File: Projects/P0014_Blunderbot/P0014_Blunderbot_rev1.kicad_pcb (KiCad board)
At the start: 2 copper layers, 63.5 x 25.4 mm, 19 parts, among them J1 22-03-5035, J2 22-03-5035, J3 70553-0037, J4 70553-0037, J5 CONN_01X04, J6 CONN_01X04, P1 CONN_02X03, U1 TC7W241FUTE12LF, U2 MIC5219-5.0YM5-TR, U3 MIC5219-5.0YM5-TR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

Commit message: layout nearly done
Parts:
- added S1: MHSS1105, Pin_Headers:Pin_Header_Straight_1x03, F.Cu at (129.5, 89.5)
- moved U3 22.5 mm to (140.6, 107.0)
- moved C2 19.7 mm to (145.3, 105.3), turned to 90 degrees
- moved RP1 18.2 mm to (137.5, 90.8)
- moved U4 14.2 mm to (151.9, 101.5), turned to 0 degrees
- moved C4 14.1 mm to (159.5, 106.6), turned to 90 degrees
- moved C5 11.8 mm to (140.2, 97.7)
- moved C1 8.52 mm to (133.4, 102.9), turned to 0 degrees
- moved U2 8.42 mm to (124.6, 95.6), turned to 180 degrees
- moved C3 4.09 mm to (124.5, 100.9), turned to 270 degrees
- moved D2 3.42 mm to (129.5, 93.3), turned to 180 degrees
- moved U1 3.32 mm to (141.4, 100.9)
- moved J5 2.54 mm to (177.8, 95.2)
- moved J6 2.54 mm to (119.4, 102.9)
- moved J3 2.54 mm to (163.8, 92.7)
- moved J4 2.54 mm to (168.9, 105.4)
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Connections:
- C1 pad 1: /9-12V_IN -> /9-10V_IN
- J1 pad 2: /9-12V_IN -> /9-10V_IN
- J2 pad 2: /9-12V_IN -> /9-10V_IN
- J3 pad 2: /MISO -> /MOSI/PWM2
- J4 pad 2: /PWM1 -> /MISO/PWM1
- P1 pad 1: /MISO -> /MISO/PWM1
- P1 pad 4: /MOSI -> /MOSI/PWM2
- U1 pad 5: /PWM1 -> /TX
- U2 pad 1: /9-12V_IN -> /9-10V_IN
- U2 pad 3: /9-12V_IN -> Net-(S1-Pad3)
- U3 pad 1: /9-12V_IN -> /9-10V_IN
- U4 pad 10: /SERVO_EN -> /TXDEN
- U4 pad 12: /PWM1 -> /TX
- U4 pad 13: /TXDEN -> /SERVO_EN
- U4 pad 7: /MOSI -> /MOSI/PWM2
- U4 pad 8: /MISO -> /MISO/PWM1
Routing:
- net GND: track 0.00 -> 148.0 mm, vias 0 -> 5
- net /VCC: track 4.39 -> 76.6 mm, vias 0 -> 2
- net /9-10V_IN: track 0.00 -> 40.6 mm, vias 0 -> 2
- net /MISO: track 35.4 -> 0.00 mm, vias 1 -> 0
- net /PWM1: track 31.9 -> 0.00 mm
- net /TTL_BUS: track 4.40 -> 36.3 mm, vias 0 -> 2
- net /MOSI/PWM2: track 0.00 -> 29.4 mm
- net /MISO/PWM1: track 0.00 -> 29.1 mm, vias 0 -> 2
- net Net-(D1-Pad1): track 0.00 -> 24.0 mm, vias 0 -> 1
- net /TRIG1: track 48.4 -> 24.5 mm
- net /VBB: track 20.0 -> 41.5 mm, vias 0 -> 1
- net /TRIG2: track 20.6 -> 33.7 mm
- net /TX: track 0.00 -> 12.6 mm, vias 0 -> 2
- net /ECHO2: track 24.6 -> 37.1 mm
- net /TXDEN: track 4.67 -> 16.9 mm
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- added copper zone on B.Cu, net /9-10V_IN
- added copper zone on B.Cu, net /VBB
- added copper zone on B.Cu, net /VCC
- added copper zone on B.Cu, net GND
- added copper zone on F.Cu, net GND
- added copper zone on B.Cu, net Net-(C3-Pad1)
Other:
- board text added: "9-10VIN"
- board text added: "Blunderbot"
- board text added: "Designed by Max Prokopenko"
- board text added: "OpenRobotics.ca"
- board text added: "P0014 rev1"
- board text added: "PA0-SERVO_EN PA1-TX PA2-RX PA3-TXDEN PA4-SCK PA5-MISO/PWM1 PA6-MOSI/PWM2 PA7-TRIG1 PB0-ECHO1 PB1-TRIG2 PB2-ECHO2 PB3-~RESET"
- board text removed: "9-11VIN"

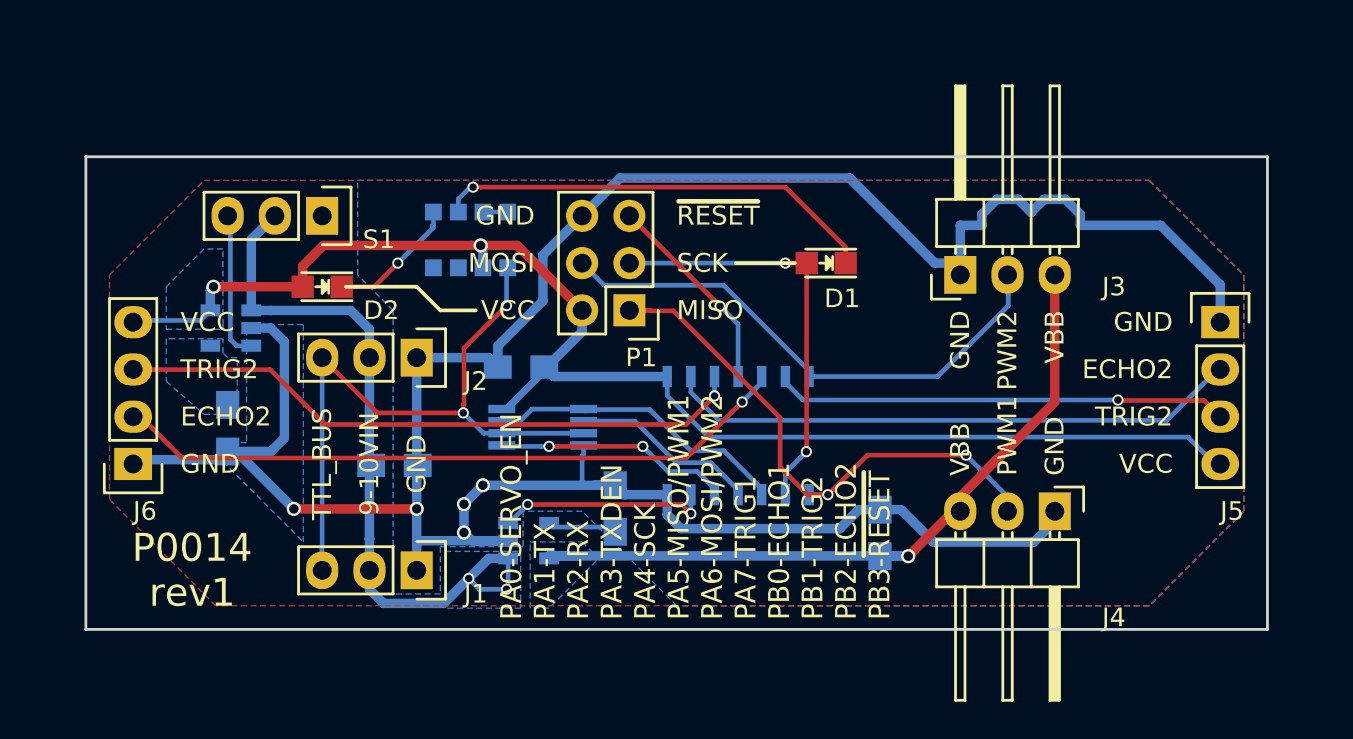
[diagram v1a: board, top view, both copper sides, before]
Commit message: layout first pass finished, need to update gerbers for seeed
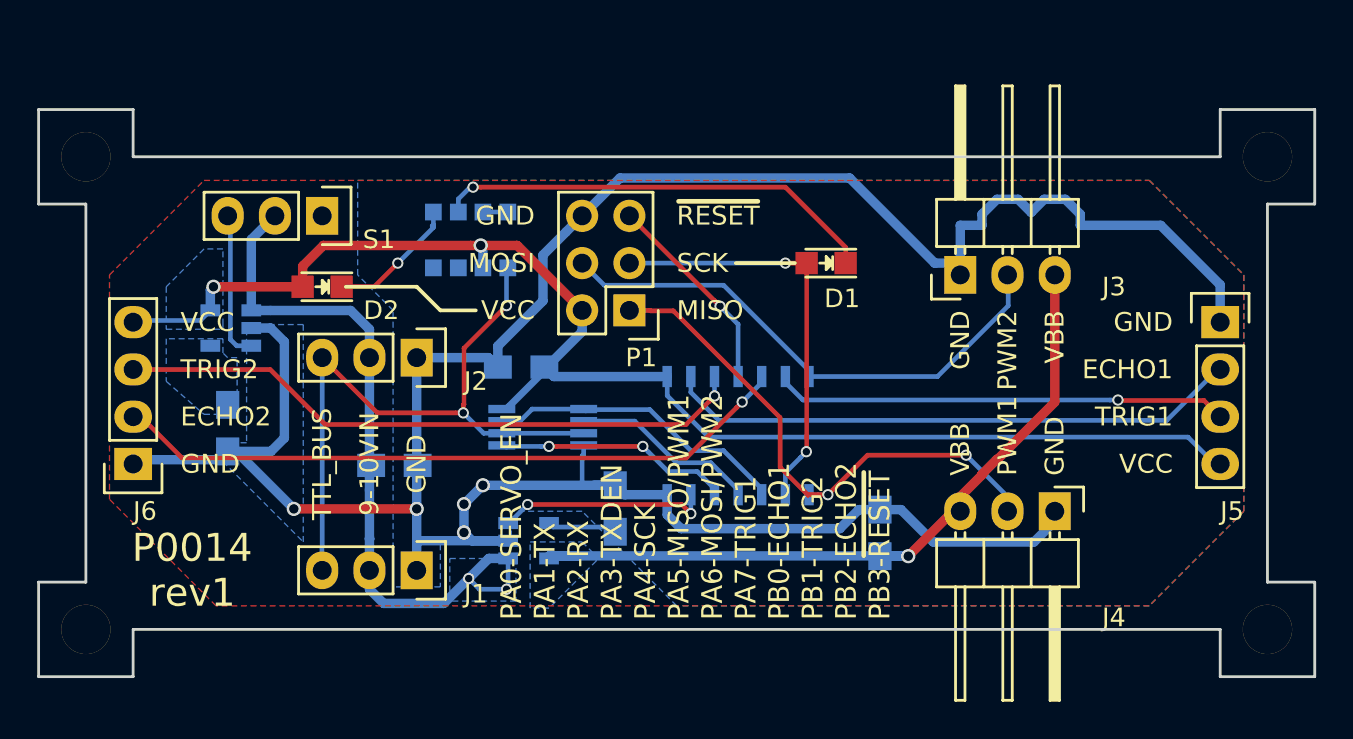
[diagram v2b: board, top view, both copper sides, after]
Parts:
- added REF**: modular8_mounting_hole, open_robotics:modular8_mounting_hole, F.Cu at (180.3, 86.4)
- added REF**: modular8_mounting_hole, open_robotics:modular8_mounting_hole, F.Cu at (180.3, 111.8)
- added REF**: modular8_mounting_hole, open_robotics:modular8_mounting_hole, F.Cu at (116.8, 111.8)
- added REF**: modular8_mounting_hole, open_robotics:modular8_mounting_hole, F.Cu at (116.8, 86.4)
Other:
- board size 63.5 x 25.4 mm -> 68.6 x 30.5 mm
- net class power: clearance 0.254 -> 0.2
- board text added: "ECHO1"
- board text added: "TRIG1"
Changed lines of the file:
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@@
 (kicad_pcb (version 4) (host pcbnew 4.0.1-stable)
   (general
-    (links 59)
+    (links 0)
     (no_connects 0)
-    (area 114.217667 79.240999 182.962334 113.799001)
+    (area 107.231666 81.834999 189.948335 116.285001)
     (thickness 1.6)
-    (drawings 37)
+    (drawings 53)
     (tracks 304)
     (zones 0)
-    (modules 20)
+    (modules 24)
     (nets 25)
   )
   (page A4)
   (layers
-    (0 F.Cu signal hide)
+    (0 F.Cu signal)
     (31 B.Cu signal)
     (32 B.Adhes user hide)
@@
     (34 B.Paste user hide)
     (35 F.Paste user hide)
-    (36 B.SilkS user)
-    (37 F.SilkS user hide)
+    (36 B.SilkS user hide)
+    (37 F.SilkS user)
     (38 B.Mask user hide)
     (39 F.Mask user hide)
@@
     (pad_to_mask_clearance 0.2)
     (aux_axis_origin 0 0)
-    (visible_elements 7FFFBE7F)
+    (visible_elements 7FFFFE7F)
     (pcbplotparams
-      (layerselection 0x00030_80000001)
-      (usegerberextensions false)
+      (layerselection 0x010f0_80000001)
+      (usegerberextensions true)
       (excludeedgelayer true)
       (linewidth 0.100000)
@@
       (outputformat 1)
       (mirror false)
-      (drillshape 1)
+      (drillshape 0)
       (scaleselection 1)
       (outputdirectory ""))
@@
   )
   (net_class power ""
-    (clearance 0.254)
+    (clearance 0.2)
     (trace_width 0.508)
     (via_dia 0.762)
@@
     )
   )
-  (gr_text Blunderbot (at 170.434 89.154) (layer B.SilkS)
+  (module open_robotics:modular8_mounting_hole (layer F.Cu)
+    (at 180.34 86.36)
+    (fp_text reference REF** (at 0 0.5) (layer F.SilkS) hide
+      (effects (font (size 1 1) (thickness 0.15)))
+    )
+    (fp_text value modular8_mounting_hole (at 0 -0.5) (layer F.Fab) hide
+      (effects (font (size 1 1) (thickness 0.15)))
+    )
+    (pad 1 thru_hole circle (at 0 0) (size 2.65 2.65) (drill 2.65) (layers *.Cu *.Mask F.SilkS))
+  )
+  (module open_robotics:modular8_mounting_hole (layer F.Cu)
+    (at 180.34 111.76)
+    (fp_text reference REF** (at 0 0.5) (layer F.SilkS) hide
+      (effects (font (size 1 1) (thickness 0.15)))
+    )
+    (fp_text value modular8_mounting_hole (at 0 -0.5) (layer F.Fab) hide
+      (effects (font (size 1 1) (thickness 0.15)))
+    )
+    (pad 1 thru_hole circle (at 0 0) (size 2.65 2.65) (drill 2.65) (layers *.Cu *.Mask F.SilkS))
+  )
+  (module open_robotics:modular8_mounting_hole (layer F.Cu)
+    (at 116.84 111.76)
+    (fp_text reference REF** (at 0 0.5) (layer F.SilkS) hide
+      (effects (font (size 1 1) (thickness 0.15)))
+    )
+    (fp_text value modular8_mounting_hole (at 0 -0.5) (layer F.Fab) hide
+      (effects (font (size 1 1) (thickness 0.15)))
+    )
+    (pad 1 thru_hole circle (at 0 0) (size 2.65 2.65) (drill 2.65) (layers *.Cu *.Mask F.SilkS))
+  )
+  (module open_robotics:modular8_mounting_hole (layer F.Cu)
+    (at 116.84 86.36)
+    (fp_text reference REF** (at 0 0.5) (layer F.SilkS) hide
+      (effects (font (size 1 1) (thickness 0.15)))
+    )
+    (fp_text value modular8_mounting_hole (at 0 -0.5) (layer F.Fab) hide
+      (effects (font (size 1 1) (thickness 0.15)))
+    )
+    (pad 1 thru_hole circle (at 0 0) (size 2.65 2.65) (drill 2.65) (layers *.Cu *.Mask F.SilkS))
+  )
+  (gr_line (start 180.34 109.22) (end 180.34 88.9) (layer Edge.Cuts) (width 0.15))
+  (gr_line (start 182.88 109.22) (end 180.34 109.22) (layer Edge.Cuts) (width 0.15))
+  (gr_line (start 182.88 114.3) (end 182.88 109.22) (layer Edge.Cuts) (width 0.15))
+  (gr_line (start 177.8 114.3) (end 182.88 114.3) (layer Edge.Cuts) (width 0.15))
+  (gr_line (start 177.8 111.76) (end 177.8 114.3) (layer Edge.Cuts) (width 0.15))
+  (gr_line (start 119.38 111.76) (end 177.8 111.76) (layer Edge.Cuts) (width 0.15))
+  (gr_line (start 119.38 114.3) (end 119.38 111.76) (layer Edge.Cuts) (width 0.15))
+  (gr_line (start 114.3 114.3) (end 119.38 114.3) (layer Edge.Cuts) (width 0.15))
+  (gr_line (start 114.3 109.22) (end 114.3 114.3) (layer Edge.Cuts) (width 0.15))
+  (gr_line (start 116.84 109.22) (end 114.3 109.22) (layer Edge.Cuts) (width 0.15))
+  (gr_line (start 116.84 88.9) (end 116.84 109.22) (layer Edge.Cuts) (width 0.15))
+  (gr_line (start 114.3 88.9) (end 116.84 88.9) (layer Edge.Cuts) (width 0.15))
+  (gr_line (start 114.3 83.82) (end 114.3 88.9) (layer Edge.Cuts) (width 0.15))
+  (gr_line (start 119.38 83.82) (end 114.3 83.82) (layer Edge.Cuts) (width 0.15))
+  (gr_line (start 119.38 86.36) (end 119.38 83.82) (layer Edge.Cuts) (width 0.15))
+  (gr_line (start 177.8 86.36) (end 119.38 86.36) (layer Edge.Cuts) (width 0.15))
+  (gr_line (start 177.8 83.82) (end 177.8 86.36) (layer Edge.Cuts) (width 0.15))
+  (gr_line (start 182.88 83.82) (end 177.8 83.82) (layer Edge.Cuts) (width 0.15))
+  (gr_line (start 182.88 88.9) (end 182.88 83.82) (layer Edge.Cuts) (width 0.15))
+  (gr_line (start 180.34 88.9) (end 182.88 88.9) (layer Edge.Cuts) (width 0.15))
+  (gr_text Blunderbot (at 169.545 89.535) (layer B.SilkS)
     (effects (font (size 2.032 2.032) (thickness 0.381)) (justify mirror))
   )
-  (gr_text "Designed by\nMax Prokopenko" (at 175.26 96.774) (layer B.SilkS)
+  (gr_text "Designed by\nMax Prokopenko" (at 175.26 99.695) (layer B.SilkS)
     (effects (font (size 1.016 1.016) (thickness 0.254)) (justify left mirror))
   )
@@
     (effects (font (size 1.5 1.5) (thickness 0.3)))
   )
-  (gr_text OpenRobotics.ca (at 169.672 109.22) (layer B.SilkS)
+  (gr_text OpenRobotics.ca (at 165.735 95.885) (layer B.SilkS)
     (effects (font (thickness 0.3048)) (justify mirror))
   )
@@
     (effects (font (size 1.016 1.016) (thickness 0.254)) (justify right))
   )
-  (gr_text TRIG2 (at 175.26 100.33) (layer F.SilkS)
+  (gr_text TRIG1 (at 175.26 100.33) (layer F.SilkS)
     (effects (font (size 1.016 1.016) (thickness 0.254)) (justify right))
   )
@@
     (effects (font (size 1.016 1.016) (thickness 0.254)) (justify right))
   )
-  (gr_text ECHO2 (at 175.26 97.79) (layer F.SilkS)
+  (gr_text ECHO1 (at 175.26 97.79) (layer F.SilkS)
     (effects (font (size 1.016 1.016) (thickness 0.254)) (justify right))
   )
@@
     (effects (font (size 1.016 1.016) (thickness 0.254)) (justify left))
   )
-  (gr_line (start 116.84 111.76) (end 180.34 111.76) (layer Edge.Cuts) (width 0.15))
-  (gr_line (start 180.34 86.36) (end 180.34 111.76) (layer Edge.Cuts) (width 0.15))
-  (gr_line (start 116.84 86.36) (end 116.84 111.76) (layer Edge.Cuts) (width 0.15))
-  (gr_line (start 116.84 86.36) (end 180.34 86.36) (layer Edge.Cuts) (width 0.15))
   (segment (start 159.512 105.323) (end 160.645 105.323) (width 0.508) (layer B.Cu) (net 1))
   (segment (start 160.645 105.323) (end 162.383 107.061) (width 0.508) (layer B.Cu) (net 1))
@@
     (polygon
       (pts
-        (xy 140.208 107.823) (xy 140.208 110.617) (xy 136.144 110.617) (xy 136.144 107.569) (xy 140.208 107.569)
+        (xy 139.954 107.95) (xy 139.954 110.236) (xy 136.398 110.236) (xy 136.398 107.95)
       )
     )
@@
     (polygon
       (pts
-        (xy 173.99 110.49) (xy 148.59 110.49) (xy 143.51 105.41) (xy 140.335 105.41) (xy 140.335 107.315)
-        (xy 135.89 107.315) (xy 135.89 109.855) (xy 133.35 109.855) (xy 133.35 94.615) (xy 131.445 92.71)
+        (xy 173.99 110.49) (xy 148.59 110.49) (xy 143.51 105.41) (xy 139.7 105.41) (xy 139.7 107.188)
+        (xy 135.89 107.188) (xy 135.89 109.474) (xy 133.35 109.474) (xy 133.35 94.615) (xy 131.445 92.71)
         (xy 131.445 87.63) (xy 173.99 87.63) (xy 179.07 92.71) (xy 179.07 105.41)
       )

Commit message: finishing routing on bus adapter
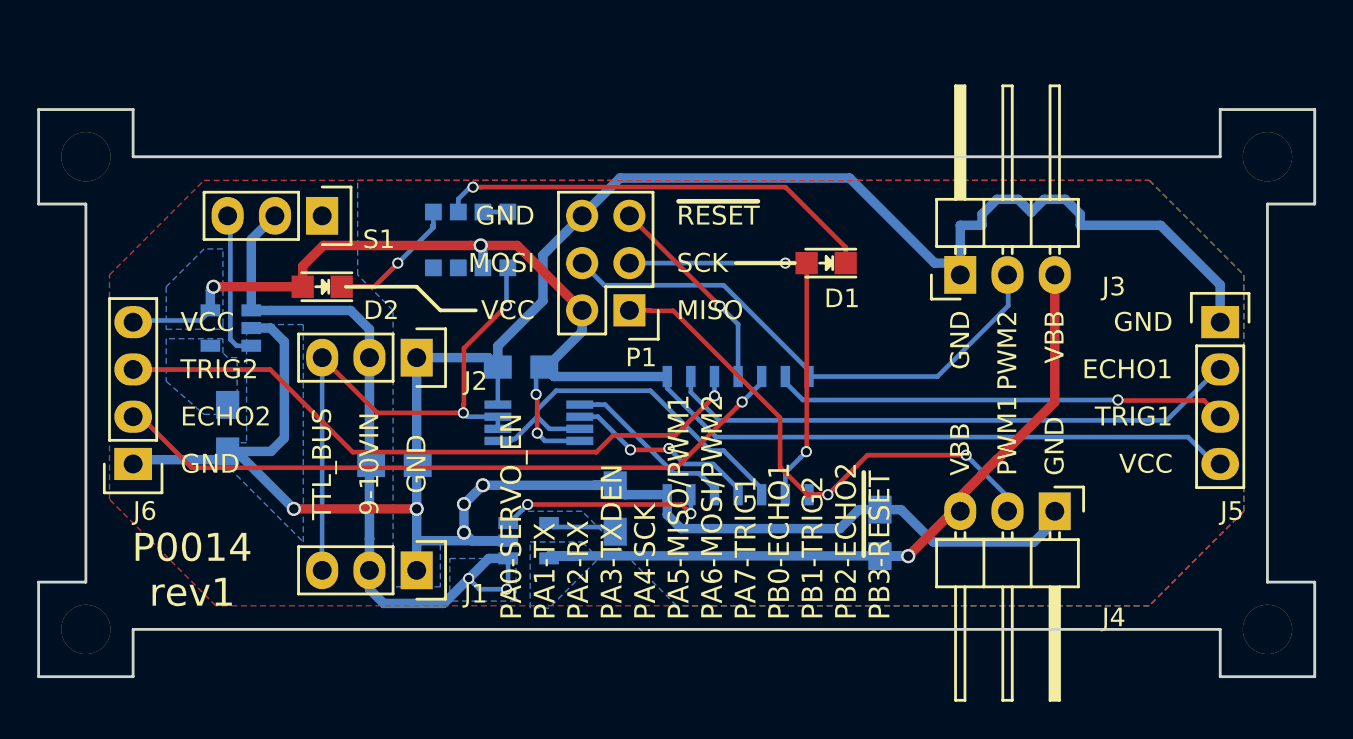
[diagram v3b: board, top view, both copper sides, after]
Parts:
- moved U1 0.32 mm to (141.2, 100.7), turned to 0 degrees
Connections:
- U1 pad 2: /RX -> /TTL_BUS
- U1 pad 6: /TTL_BUS -> /RX
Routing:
- net /TTL_BUS: track 36.3 -> 31.9 mm
- net /TXDEN: track 16.9 -> 20.9 mm
- net /VCC: track 76.6 -> 79.8 mm, vias 2 -> 4
- net /TX: track 12.6 -> 9.43 mm, vias 2 -> 0
- net /TRIG2: track 33.7 -> 34.9 mm
- net /RX: track 10.4 -> 10.5 mm, vias 0 -> 2
